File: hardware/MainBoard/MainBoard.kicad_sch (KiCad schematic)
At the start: 26 parts, among them J1 Conn_02x16_Top_Bottom, J2 Conn_02x16_Top_Bottom, J7 Conn_02x16_Top_Bottom, Q1 MMBT2222A, U1 ESP32-S3-WROOM-1, U2 AMS1117-3.3, U3 AMS1117-5.0

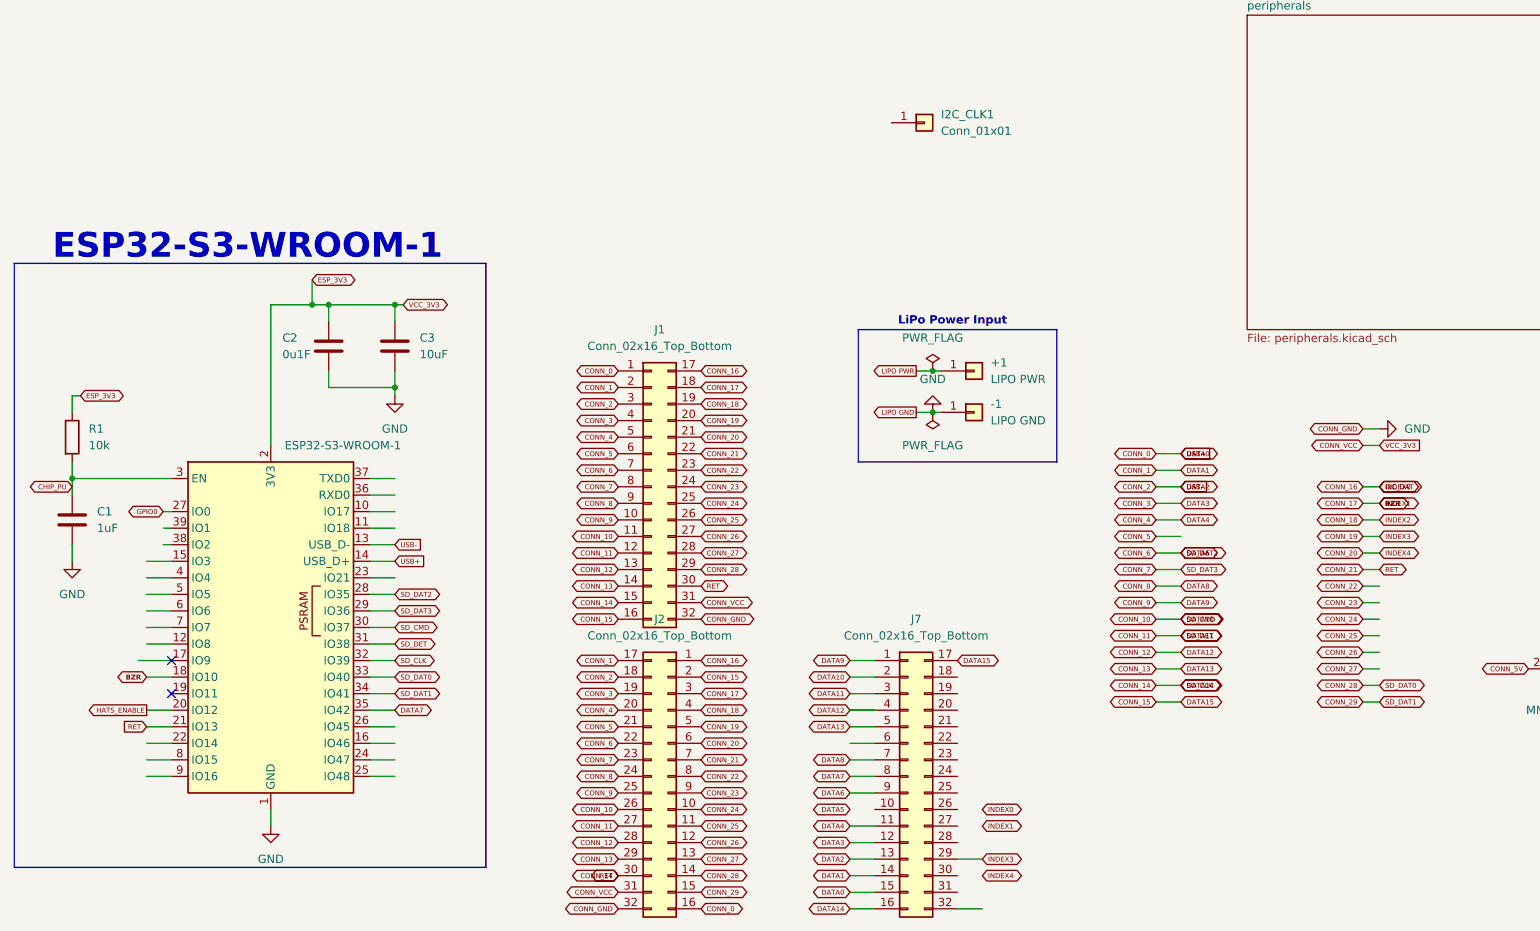
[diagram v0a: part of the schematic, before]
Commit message: replaced files with backup - were broken
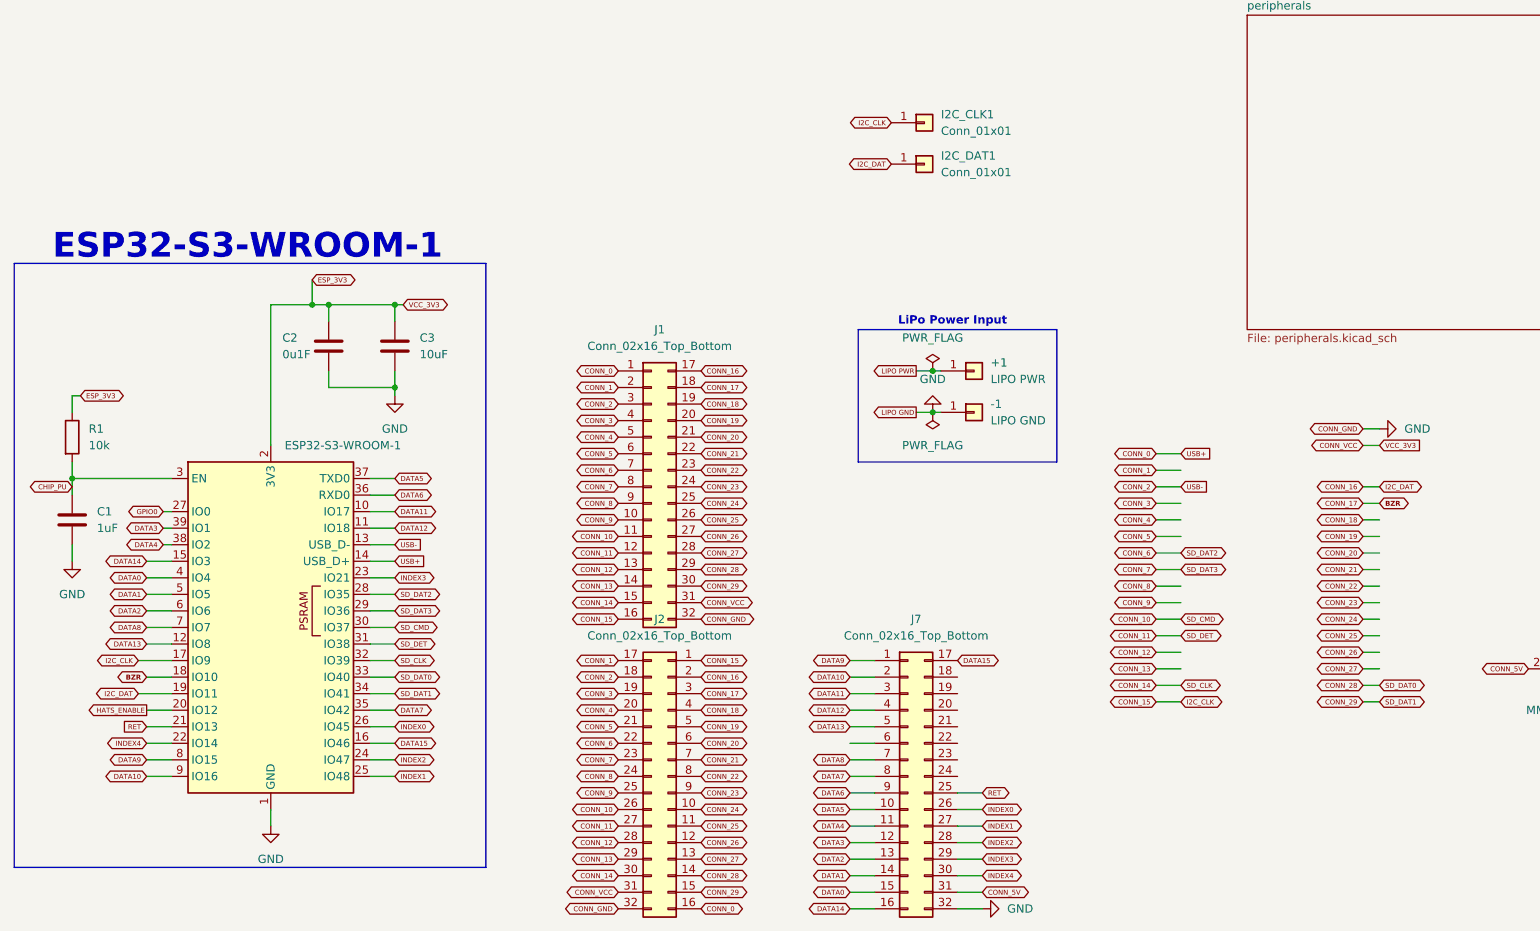
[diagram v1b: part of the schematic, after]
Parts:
- added I2C_DAT1: Conn_01x01, TestPoint:TestPoint_Pad_1.0x1.0mm, symbol Connector_Generic:Conn_01x01
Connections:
- net CONN_0: no longer J7.15 (Pin_15)
- net CONN_1: no longer J7.14 (Pin_14)
- net CONN_10: no longer J7.2 (Pin_2)
- net CONN_11: no longer J7.3 (Pin_3)
- net CONN_12: no longer J7.4 (Pin_4)
- net CONN_13: no longer J7.5 (Pin_5)
- net CONN_14: no longer J1.22 (Pin_22), J1.30 (Pin_30), J2.7 (Pin_7), J7.16 (Pin_16), U1.21 (IO13)
- net CONN_15: now also I2C_CLK1.1 (Pin_1), J2.1 (Pin_1), U1.17 (IO9); no longer J2.2 (Pin_2), J7.17 (Pin_17)
- net CONN_16: now also J2.2 (Pin_2), U1.19 (IO11), I2C_DAT1.1 (Pin_1); no longer J2.1 (Pin_1)
- net CONN_19: no longer J7.29 (Pin_29)
- net CONN_2: no longer J7.13 (Pin_13)
- net CONN_29: now also J1.30 (Pin_30)
- net CONN_3: no longer J7.12 (Pin_12)
- net CONN_4: no longer J7.11 (Pin_11)
- net CONN_5V: now also J7.31 (Pin_31)
- net CONN_6: no longer J7.9 (Pin_9)
- net CONN_8: no longer J7.7 (Pin_7)
- net CONN_9: no longer J7.1 (Pin_1)
- net DATA5: now also J7.10 (Pin_10), U1.37 (TXD0)
- net GND: now also J7.32 (Pin_32)
- net RET: now reaches J7.25 (Pin_25)
- net RET: now also U1.21 (IO13)
- net INDEX0: now reaches J7.26 (Pin_26)
- net INDEX0: now also U1.26 (IO45)
- net INDEX1: now reaches J7.27 (Pin_27)
- net INDEX1: now also U1.25 (IO48)
- net INDEX2: now reaches J7.28 (Pin_28)
- net INDEX2: now also U1.24 (IO47)
- net INDEX4: now reaches J7.30 (Pin_30)
- net INDEX4: now also U1.22 (IO14)
- net DATA11: now reaches U1.10 (IO17)
- net DATA11: now also J7.3 (Pin_3)
- net DATA12: now reaches U1.11 (IO18)
- net DATA12: now also J7.4 (Pin_4)
- net DATA13: now reaches U1.12 (IO8)
- net DATA13: now also J7.5 (Pin_5)
- net DATA14: now reaches U1.15 (IO3)
- net DATA14: now also J7.16 (Pin_16)
- net DATA15: now reaches U1.16 (IO46)
- net DATA15: now also J7.17 (Pin_17)
- net INDEX3: now reaches U1.23 (IO21)
- net INDEX3: now also J7.29 (Pin_29)
- net DATA6: now reaches U1.36 (RXD0)
- net DATA6: now also J7.9 (Pin_9)
- net DATA4: now reaches U1.38 (IO2)
- net DATA4: now also J7.11 (Pin_11)
- net DATA3: now reaches U1.39 (IO1)
- net DATA3: now also J7.12 (Pin_12)
- net DATA0: now reaches U1.4 (IO4)
- net DATA0: now also J7.15 (Pin_15)
- net DATA1: now reaches U1.5 (IO5)
- net DATA1: now also J7.14 (Pin_14)
- net DATA2: now reaches U1.6 (IO6)
- net DATA2: now also J7.13 (Pin_13)
- net DATA8: now reaches U1.7 (IO7)
- net DATA8: now also J7.7 (Pin_7)
- net DATA9: now reaches U1.8 (IO15)
- net DATA9: now also J7.1 (Pin_1)
- net DATA10: now reaches U1.9 (IO16)
- net DATA10: now also J7.2 (Pin_2)
- new net CONN_21: J1.22 (Pin_22), J2.7 (Pin_7)
- no-connect marks 2 -> 0

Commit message: finished main board w/ ground and power planes
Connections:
- net CONN_VCC: no longer C10.1, C11.1, Q1.3 (C), R3.1, U3.2 (VO)
- new net VCC_5V: C10.1, C11.1, Q1.3 (C), R3.1, U3.2 (VO)
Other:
- note removed: "Hat Connection Interface"
- moved on the sheet: C10, C11, C4, C5, C6, C7, C8, C9, D1, D2, I2C_CLK1, I2C_DAT1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

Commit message: added voltage switcher - still needs to be routed
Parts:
- added Q2, Q3: FDN340P, Package_TO_SOT_SMD:SOT-23, symbol Transistor_FET:FDN340P
- added R13: 10K, symbol Device:R_Small
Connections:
- net CONN_5V: no longer J7.31 (Pin_31)
- net CONN_VCC: no longer C2.1, C3.1, C6.1, C7.1, J2.31 (Pin_31), R1.1, R2.1, U1.2 (3V3), U2.2 (VO)
- net GND: now also R13.2
- net LIPO PWR: now also Q3.3 (D), R13.1; no longer C4.1, C5.1, C8.1, C9.1, U2.3 (VI), U3.3 (VI)
- net VCC_5V: now also J2.31 (Pin_31), J7.31 (Pin_31)
- new net +5V: Q2.2 (S), Q3.1 (G)
- new net ESP_3V3: C2.1, C3.1, C6.1, C7.1, R1.1, R2.1, U1.2 (3V3), U2.2 (VO)
- new net LIPO_PWR: Q2.1 (G)
- new net VBUS: Q2.3 (D)
- new net VIN: C4.1, C5.1, C8.1, C9.1, Q3.2 (S), U2.3 (VI), U3.3 (VI)
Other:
- note added: "Voltage Selector"
- moved on the sheet: C10, C11, C8, C9, D2, R3, U3

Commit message: added USB power switching
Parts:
- R13: footprint (none) -> Resistor_SMD:R_0603_1608Metric
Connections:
- net CONN_20 is gone; now on net CONN_19: J1.21 (Pin_21), J2.6 (Pin_6)
- net CONN_21 is gone; now on net CONN_19: J1.22 (Pin_22), J2.7 (Pin_7)
- net CONN_22 is gone; now on net CONN_19: J1.23 (Pin_23), J2.8 (Pin_8)
- net CONN_23 is gone; now on net CONN_19: J1.24 (Pin_24), J2.9 (Pin_9)
- net CONN_24 is gone; now on net CONN_19: J1.25 (Pin_25), J2.10 (Pin_10)
- net CONN_25 is gone; now on net CONN_19: J1.26 (Pin_26), J2.11 (Pin_11)
- net CONN_4 is gone; now on net BZR: J1.5 (Pin_5), J2.20 (Pin_20)
- net CONN_VCC is gone; now on net VIN: J1.31 (Pin_31)
- net ESP_3V3 is gone; now on net CONN_19: C2.1, C3.1, C6.1, C7.1, R1.1, R2.1, U1.2 (3V3), U2.2 (VO)
- net LIPO_PWR is gone; now on net LIPO PWR: Q2.1 (G)
- net BZR: no longer J1.18 (Pin_18), J2.3 (Pin_3)
- net VCC_5V: no longer J2.31 (Pin_31)
- net VIN: now also J2.31 (Pin_31)
- new net CONN_17: J1.18 (Pin_18), J2.3 (Pin_3)
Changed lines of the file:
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@@
 	(wire
 		(pts
-			(xy 25.4 62.23) (xy 29.21 62.23)
+			(xy 25.4 62.23) (xy 27.94 62.23)
 		)
 		(stroke
@@
 		)
 	)
+	(global_label "VCC_3V3"
+		(shape input)
+		(at 227.33 147.32 0)
+		(fields_autoplaced yes)
+		(effects
+			(font
+				(size 0.762 0.762)
+				(thickness 0.254)
+				(bold yes)
+			)
+			(justify left)
+		)
+		(property "Intersheetrefs" "${INTERSHEET_REFS}"
+			(at 234.4596 147.32 0)
+			(effects
+				(font
+					(size 1.27 1.27)
+				)
+				(justify left)
+				(hide yes)
+			)
+		)
+	)
 	(global_label "ESP_3V3"
 		(shape bidirectional)
@@
 	)
 	(global_label "VIN"
-		(shape input)
+		(shape output)
 		(at 92.71 26.67 0)
 		(fields_autoplaced yes)
@@
 		)
 	)
+	(global_label "VCC_3V3"
+		(shape input)
+		(at 227.33 152.4 0)
+		(fields_autoplaced yes)
+		(effects
+			(font
+				(size 0.762 0.762)
+				(thickness 0.254)
+				(bold yes)
+			)
+			(justify left)
+		)
+		(property "Intersheetrefs" "${INTERSHEET_REFS}"
+			(at 234.4596 152.4 0)
+			(effects
+				(font
+					(size 1.27 1.27)
+				)
+				(justify left)
+				(hide yes)
+			)
+		)
+	)
 	(global_label "CONN_1"
 		(shape bidirectional)
@@
 	(global_label "VIN"
 		(shape input)
-		(at 29.21 62.23 0)
+		(at 27.94 62.23 0)
 		(fields_autoplaced yes)
 		(effects
@@
 		)
 		(property "Intersheetrefs" "${INTERSHEET_REFS}"
-			(at 35.2191 62.23 0)
+			(at 33.9491 62.23 0)
 			(effects
 				(font
@@
 		)
 	)
-	(global_label "CONN_VCC"
+	(global_label "VIN"
 		(shape bidirectional)
 		(at 123.19 147.32 0)
@@
 		)
 		(property "Intersheetrefs" "${INTERSHEET_REFS}"
-			(at 131.5628 147.32 0)
+			(at 127.4625 147.32 0)
 			(effects
 				(font
@@
 		)
 	)
-	(global_label "LIPO_PWR"
+	(global_label "LIPO PWR"
 		(shape input)
 		(at 36.83 24.13 180)
@@
 		)
 	)
+	(global_label "VCC_3V3"
+		(shape input)
+		(at 227.33 149.86 0)
+		(fields_autoplaced yes)
+		(effects
+			(font
+				(size 0.762 0.762)
+				(thickness 0.254)
+				(bold yes)
+			)
+			(justify left)
+		)
+		(property "Intersheetrefs" "${INTERSHEET_REFS}"
+			(at 234.4596 149.86 0)
+			(effects
+				(font
+					(size 1.27 1.27)
+				)
+				(justify left)
+				(hide yes)
+			)
+		)
+	)
 	(global_label "DATA6"
 		(shape bidirectional)
@@
 		)
 	)
+	(global_label "VCC_3V3"
+		(shape input)
+		(at 227.33 144.78 0)
+		(fields_autoplaced yes)
+		(effects
+			(font
+				(size 0.762 0.762)
+				(thickness 0.254)
+				(bold yes)
+			)
+			(justify left)
+		)
+		(property "Intersheetrefs" "${INTERSHEET_REFS}"
+			(at 234.4596 144.78 0)
+			(effects
+				(font
+					(size 1.27 1.27)
+				)
+				(justify left)
+				(hide yes)
+			)
+		)
+	)
 	(global_label "HATS_ENABLE"
 		(shape input)
@@
 		)
 	)
+	(global_label "VCC_3V3"
+		(shape input)
+		(at 227.33 139.7 0)
+		(fields_autoplaced yes)
+		(effects
+			(font
+				(size 0.762 0.762)
+				(thickness 0.254)
+				(bold yes)
+			)
+			(justify left)
+		)
+		(property "Intersheetrefs" "${INTERSHEET_REFS}"
+			(at 234.4596 139.7 0)
+			(effects
+				(font
+					(size 1.27 1.27)
+				)
+				(justify left)
+				(hide yes)
+			)
+		)
+	)
 	(global_label "CONN_7"
 		(shape bidirectional)
@@
 		)
 	)
-	(global_label "VCC_5V"
+	(global_label "VIN"
 		(shape bidirectional)
 		(at 110.49 191.77 180)
@@
 		)
 		(property "Intersheetrefs" "${INTERSHEET_REFS}"
-			(at 103.8953 191.77 0)
+			(at 106.2175 191.77 0)
 			(effects
 				(font
@@
 		)
 	)
+	(global_label "VCC_3V3"
+		(shape input)
+		(at 227.33 137.16 0)
+		(fields_autoplaced yes)
+		(effects
+			(font
+				(size 0.762 0.762)
+				(thickness 0.254)
+				(bold yes)
+			)
+			(justify left)
+		)
+		(property "Intersheetrefs" "${INTERSHEET_REFS}"
+			(at 234.4596 137.16 0)
+			(effects
+				(font
+					(size 1.27 1.27)
+				)
+				(justify left)
+				(hide yes)
+			)
+		)
+	)
+	(global_label "VCC_3V3"
+		(shape input)
+		(at 227.33 142.24 0)
+		(fields_autoplaced yes)
+		(effects
+			(font
+				(size 0.762 0.762)
+				(thickness 0.254)
+				(bold yes)
+			)
+			(justify left)
+		)
+		(property "Intersheetrefs" "${INTERSHEET_REFS}"
+			(at 234.4596 142.24 0)
+			(effects
+				(font
+					(size 1.27 1.27)
+				)
+				(justify left)
+				(hide yes)
+			)
+		)
+	)
 	(global_label "CONN_23"
 		(shape bidirectional)
@@
 	(global_label "BZR"
 		(shape bidirectional)
-		(at 227.33 132.08 0)
+		(at 196.85 134.62 0)
 		(fields_autoplaced yes)
 		(effects
@@
 		)
 		(property "Intersheetrefs" "${INTERSHEET_REFS}"
-			(at 232.3234 132.08 0)
+			(at 201.8434 134.62 0)
 			(effects
 				(font
@@
 			)
 		)
-		(property "Footprint" ""
+		(property "Footprint" "Resistor_SMD:R_0603_1608Metric"
 			(at 72.39 33.02 0)
 			(effects

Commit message: added power passthrough via data pins WTFFFF
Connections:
- net CONN_19: now also J7.23 (Pin_23), J7.24 (Pin_24), J7.25 (Pin_25)
- net GND: now also J1.31 (Pin_31), J2.31 (Pin_31), J7.18 (Pin_18), J7.19 (Pin_19), J7.31 (Pin_31)
- net RET: now also J7.6 (Pin_6); no longer J7.25 (Pin_25)
- net VCC_5V: now also J7.20 (Pin_20), J7.21 (Pin_21), J7.22 (Pin_22); no longer J7.31 (Pin_31)
- net VIN: no longer J1.31 (Pin_31), J2.31 (Pin_31)

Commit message: fixed main hat
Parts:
- removed D2: PWRLED, LED_SMD:LED_0603_1608Metric, symbol Device:LED
- removed Q1: MMBT2222A, Package_TO_SOT_SMD:SOT-23W, symbol Transistor_BJT:MMBT2222A
- removed R3: 75, Resistor_SMD:R_0603_1608Metric, symbol Device:R_Small
- added U4, U5: TPS22917DBV, Package_TO_SOT_SMD:SOT-23-6, symbol Power_Management:TPS22917DBV
- U1: footprint RF_Module:ESP32-S3-WROOM-1 -> RF_Module:ESP32-S3-WROOM-1U
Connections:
- net VIN is gone; now on net CONN_21: C4.1, C5.1, C8.1, C9.1, Q3.2 (S), U2.3 (VI), U3.3 (VI)
- net CONN_18: now also C2.1, C3.1, C6.1, C7.1, J1.20 (Pin_20), J1.21 (Pin_21), J2.5 (Pin_5), J2.6 (Pin_6), R1.1, R2.1, U1.2 (3V3), U2.2 (VO), U4.1 (VIN)
- net CONN_5V: now also J7.20 (Pin_20), J7.21 (Pin_21), J7.22 (Pin_22), U5.6 (VOUT)
- net GND: now also U4.2 (GND), U5.2 (GND)
- net HATS_ENABLE: now also U4.3 (ON), U5.3 (ON)
- net VCC_5V: now also U5.1 (VIN); no longer J7.20 (Pin_20), J7.21 (Pin_21), J7.22 (Pin_22)
- removed net CONN_19: C2.1, C3.1, C6.1, C7.1, J1.20 (Pin_20), J1.21 (Pin_21), J1.22 (Pin_22), J1.23 (Pin_23), J1.24 (Pin_24), J1.25 (Pin_25), J1.26 (Pin_26), J2.10 (Pin_10), J2.11 (Pin_11), J2.5 (Pin_5), J2.6 (Pin_6), J2.7 (Pin_7), J2.8 (Pin_8), J2.9 (Pin_9), J7.23 (Pin_23), J7.24 (Pin_24), J7.25 (Pin_25), R1.1, R2.1, U1.2 (3V3), U2.2 (VO)
- net CONN_26 renamed CONN_21
- net CONN_21: now also J1.22 (Pin_22), J1.23 (Pin_23), J1.24 (Pin_24), J1.25 (Pin_25), J1.26 (Pin_26), J2.10 (Pin_10), J2.11 (Pin_11), J2.7 (Pin_7), J2.8 (Pin_8), J2.9 (Pin_9)
- new net CONN_3V3: J7.23 (Pin_23), J7.24 (Pin_24), J7.25 (Pin_25), U4.6 (VOUT)
- no-connect marks 0 -> 4
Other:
- note added: "Hat Load Switches"
